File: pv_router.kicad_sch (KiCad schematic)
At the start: 0 parts

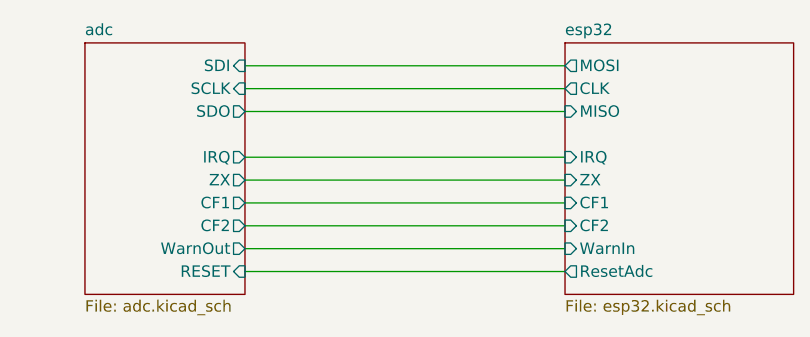
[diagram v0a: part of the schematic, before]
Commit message: feat: substitute esp32-c3 with esp32-s3
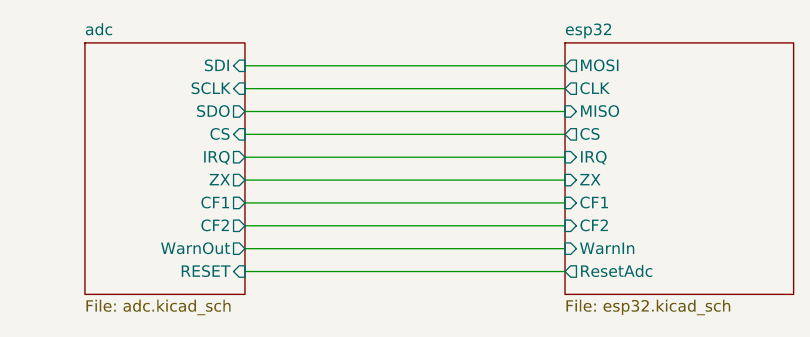
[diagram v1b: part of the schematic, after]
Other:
- sheet adc ports: added CS; removed none
- sheet esp32 ports: added CS; removed none
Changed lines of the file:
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@@
+	(wire
+		(pts
+			(xy 165.1 99.06) (xy 200.66 99.06)
+		)
+		(stroke
+			(width 0)
+			(type default)
+		)
+	)
 	(wire
 		(pts
@@
 			)
 		)
+		(pin "CS" output
+			(at 200.66 99.06 180)
+			(effects
+				(font
+					(size 1.27 1.27)
+				)
+				(justify left)
+			)
+		)
 		(instances
 			(project "pv_router"
@@
 			(effects
 				(font
+					(size 1.27 1.27)
+				)
+				(justify right)
+			)
+		)
+		(pin "CS" input
+			(at 165.1 99.06 0)
+			(effects
+				(font

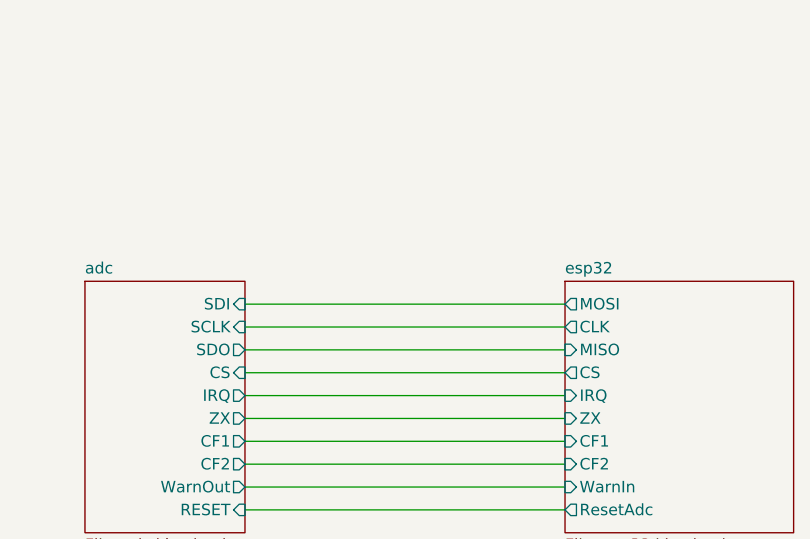
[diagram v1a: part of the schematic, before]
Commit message: feat: add SPI bus test points
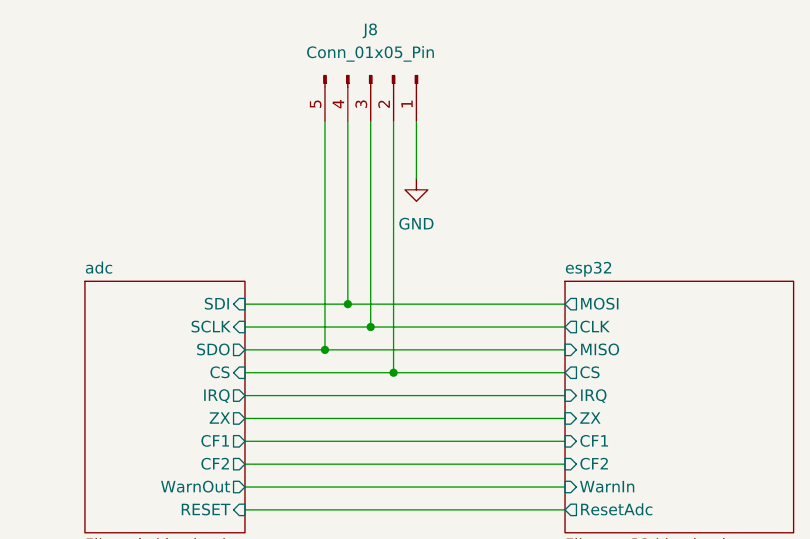
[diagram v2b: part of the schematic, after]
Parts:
- added J8: Conn_01x05_Pin, Connector_PinHeader_2.54mm:PinHeader_1x05_P2.54mm_Vertical, symbol Connector:Conn_01x05_Pin
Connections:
- net adc/CS: now also J8.2 (Pin_2)
- net adc/SCLK: now also J8.3 (Pin_3)
- net adc/SDI: now also J8.4 (Pin_4)
- net adc/SDO: now also J8.5 (Pin_5)
- new net GND: J8.1 (Pin_1)

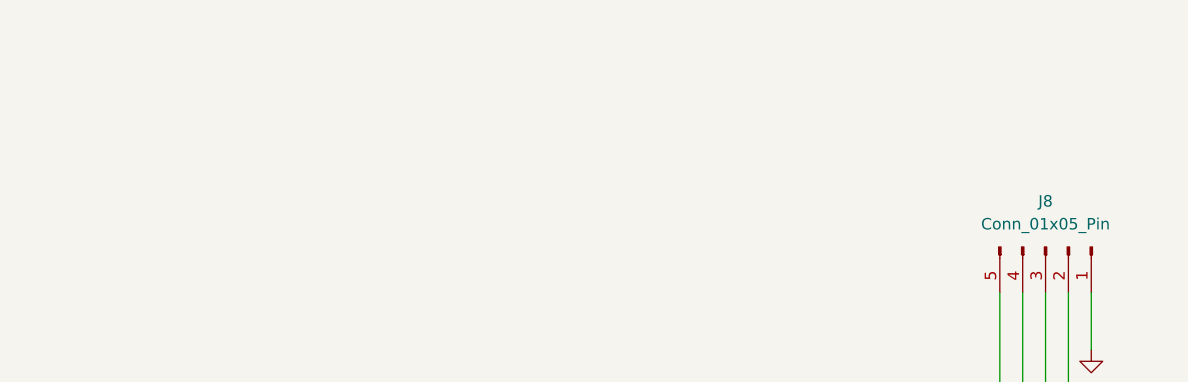
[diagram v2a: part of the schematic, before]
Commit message: fix: mounting hole to GND
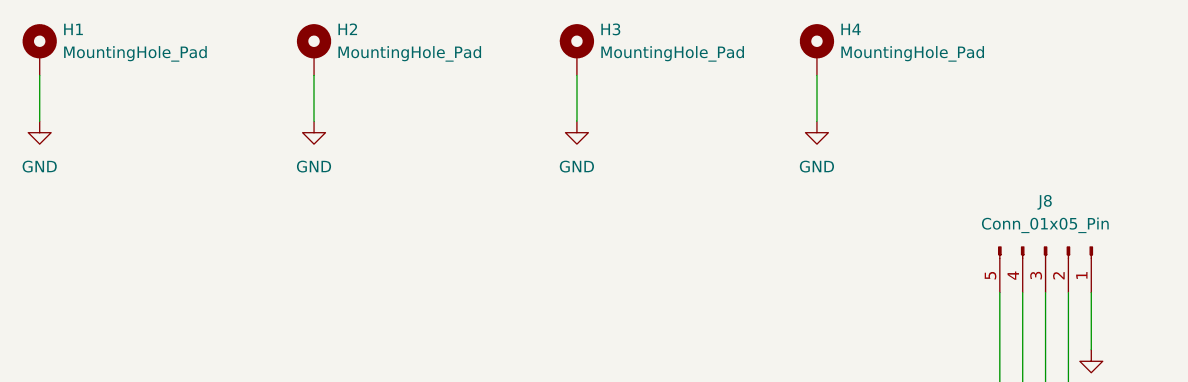
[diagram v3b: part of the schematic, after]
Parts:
- added H1, H2, H3, H4: MountingHole_Pad, MountingHole:MountingHole_2.7mm_Pad_Via, symbol Mechanical:MountingHole_Pad
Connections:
- net GND: now also H1.1, H2.1, H3.1, H4.1

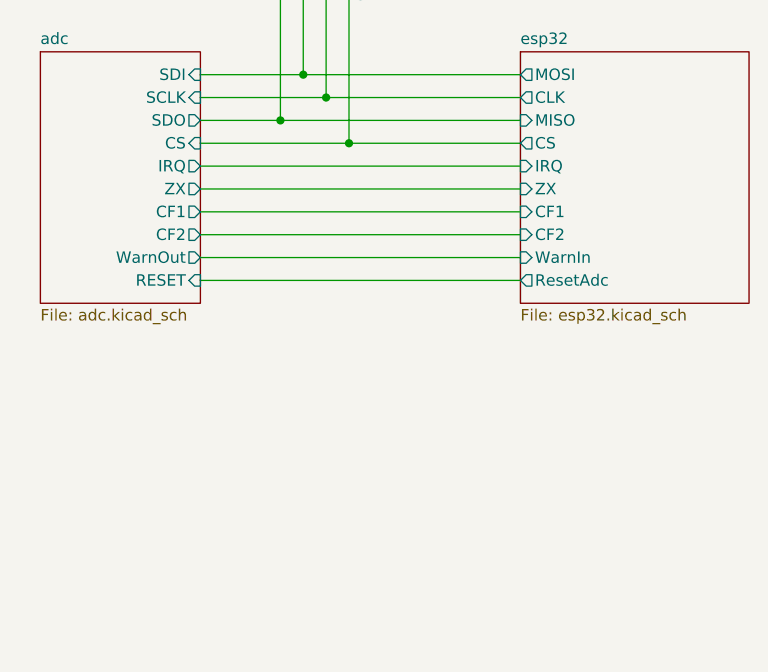
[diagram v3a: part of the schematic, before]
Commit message: feat: add test points on ESP/CAN bus
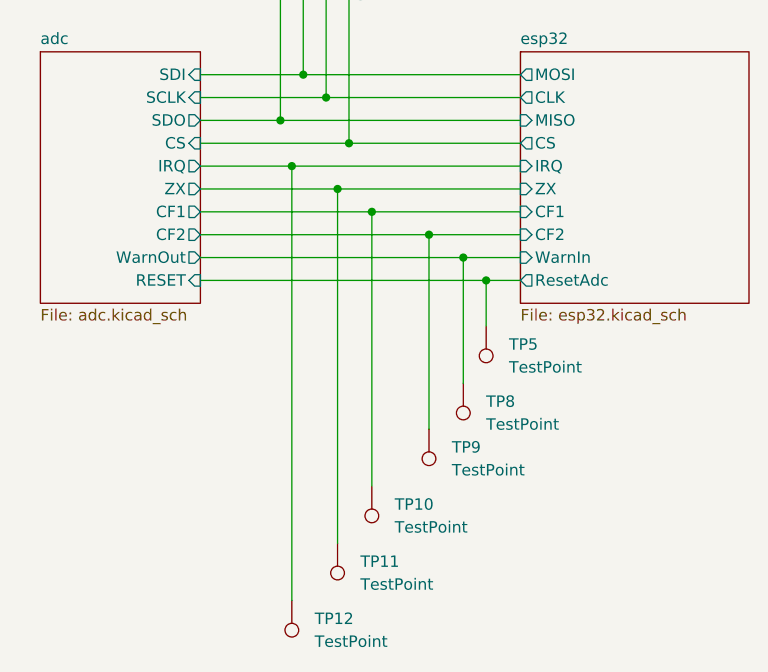
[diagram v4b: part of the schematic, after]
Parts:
- added TP10, TP11, TP12, TP5, TP8, TP9: TestPoint, TestPoint:TestPoint_Pad_D1.0mm, symbol Connector:TestPoint
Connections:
- net adc/CF1: now also TP10.1
- net adc/CF2: now also TP9.1
- net adc/IRQ: now also TP12.1
- net adc/RESET: now also TP5.1
- net adc/WarnOut: now also TP8.1
- net adc/ZX: now also TP11.1

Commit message: fix: mounting hole w/o pads
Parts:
- H1, H2, H3, H4: footprint MountingHole:MountingHole_2.7mm_Pad_Via -> MountingHole:MountingHole_2.7mm_Pad
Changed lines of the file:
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@@
 			)
 		)
-		(property "Footprint" "MountingHole:MountingHole_2.7mm_Pad_Via"
+		(property "Footprint" "MountingHole:MountingHole_2.7mm_Pad"
 			(at 127 44.45 0)
 			(effects
@@
 			)
 		)
-		(property "Footprint" "MountingHole:MountingHole_2.7mm_Pad_Via"
+		(property "Footprint" "MountingHole:MountingHole_2.7mm_Pad"
 			(at 67.31 44.45 0)
 			(effects
@@
 			)
 		)
-		(property "Footprint" "MountingHole:MountingHole_2.7mm_Pad_Via"
+		(property "Footprint" "MountingHole:MountingHole_2.7mm_Pad"
 			(at 97.79 44.45 0)
 			(effects
@@
 			)
 		)
-		(property "Footprint" "MountingHole:MountingHole_2.7mm_Pad_Via"
+		(property "Footprint" "MountingHole:MountingHole_2.7mm_Pad"
 			(at 153.67 44.45 0)
 			(effects
